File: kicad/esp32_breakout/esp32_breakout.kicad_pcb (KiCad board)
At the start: 2 copper layers, 85 x 39 mm, 29 parts, among them J1 JST PH F, J10 JST PH F, J11 JST PH F, J12 JST PH F, J13 JST PH F, J14 JST PH F, J2 JST PH F, J3 JST PH F, J4 DC-005 5.5x2.1mm, J5 Deans T-Plug M, J6 Header F, J7 Header F, J8 Header F, J9 JST PH F, Q1 BSS123, SW1 SS12D10, U1 ESP32 DEV KIT 30-pin, U2 Mini560-Pro

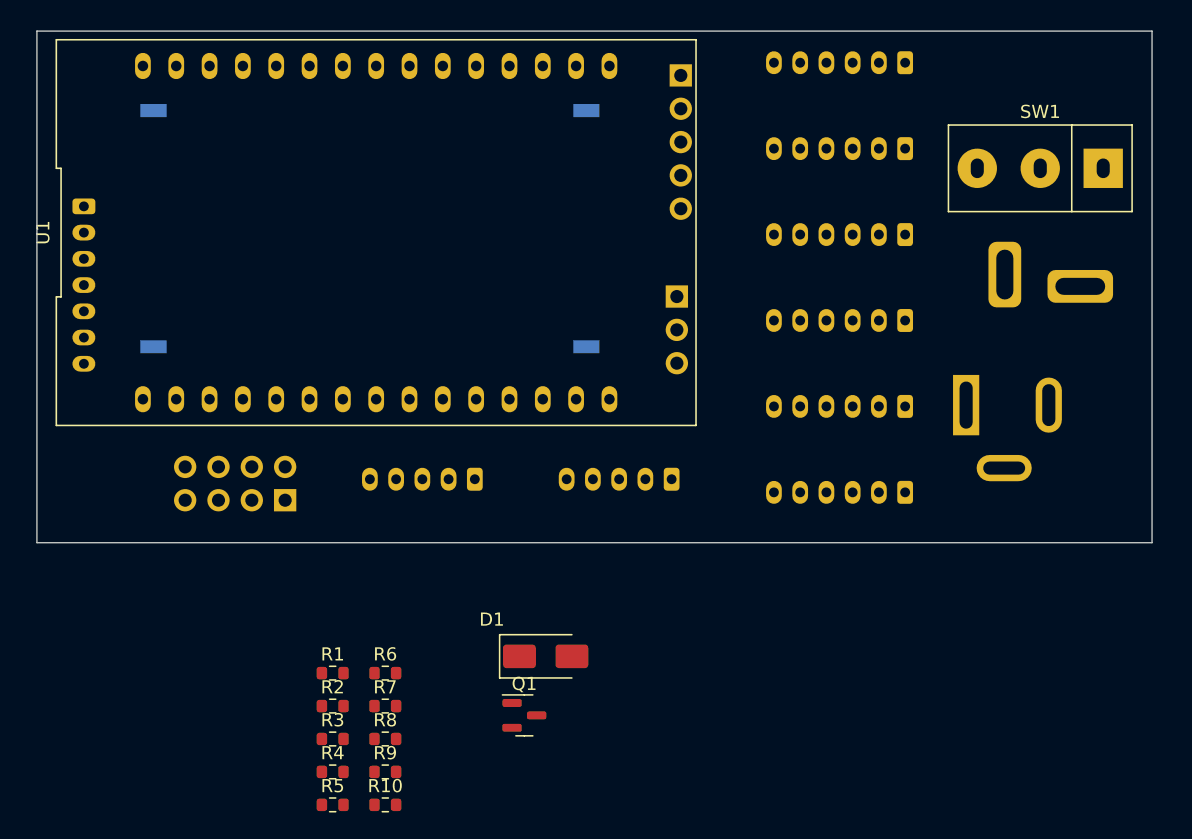
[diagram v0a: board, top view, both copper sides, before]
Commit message: Fix broken fw; ESP32 schematic
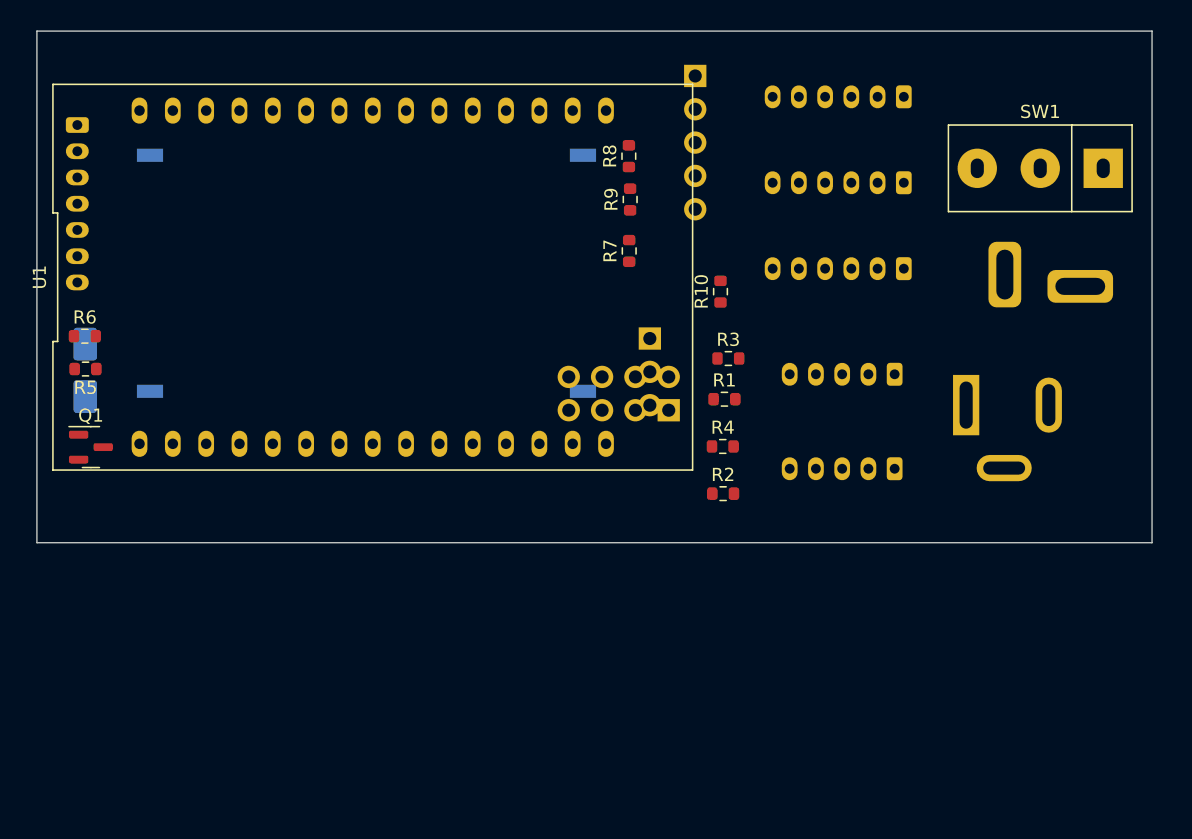
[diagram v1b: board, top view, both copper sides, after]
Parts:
- removed J12, J13, J14: JST PH F, Connector_JST:JST_PH_B6B-PH-K_1x06_P2.00mm_Vertical
- D1: moved to B.Cu
- moved R8 48.1 mm to (155.1, 87.4), turned to 90 degrees
- moved R9 47.5 mm to (155.2, 90.7), turned to 90 degrees
- moved R10 46.7 mm to (162.1, 97.7), turned to 90 degrees
- moved R3 41.8 mm to (162.7, 102.8)
- moved D1 41.3 mm to (113.7, 103.7), turned to 90 degrees
- moved R7 39.4 mm to (155.2, 94.6), turned to 90 degrees
- moved Q1 38.9 mm to (114.1, 109.5)
- moved R4 38.7 mm to (162.3, 109.5)
- moved R5 38.2 mm to (113.7, 103.6), turned to 180 degrees
- moved R1 36.4 mm to (162.4, 105.9)
- moved R6 34.4 mm to (113.7, 101.1)
- moved R2 33.9 mm to (162.3, 113.1)
- moved J1 32.0 mm to (175.4, 111.2)
- moved J6 30.0 mm to (158.2, 106.7)
- moved J2 18.8 mm to (175.4, 104.0)
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
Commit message: Layout DRC pass
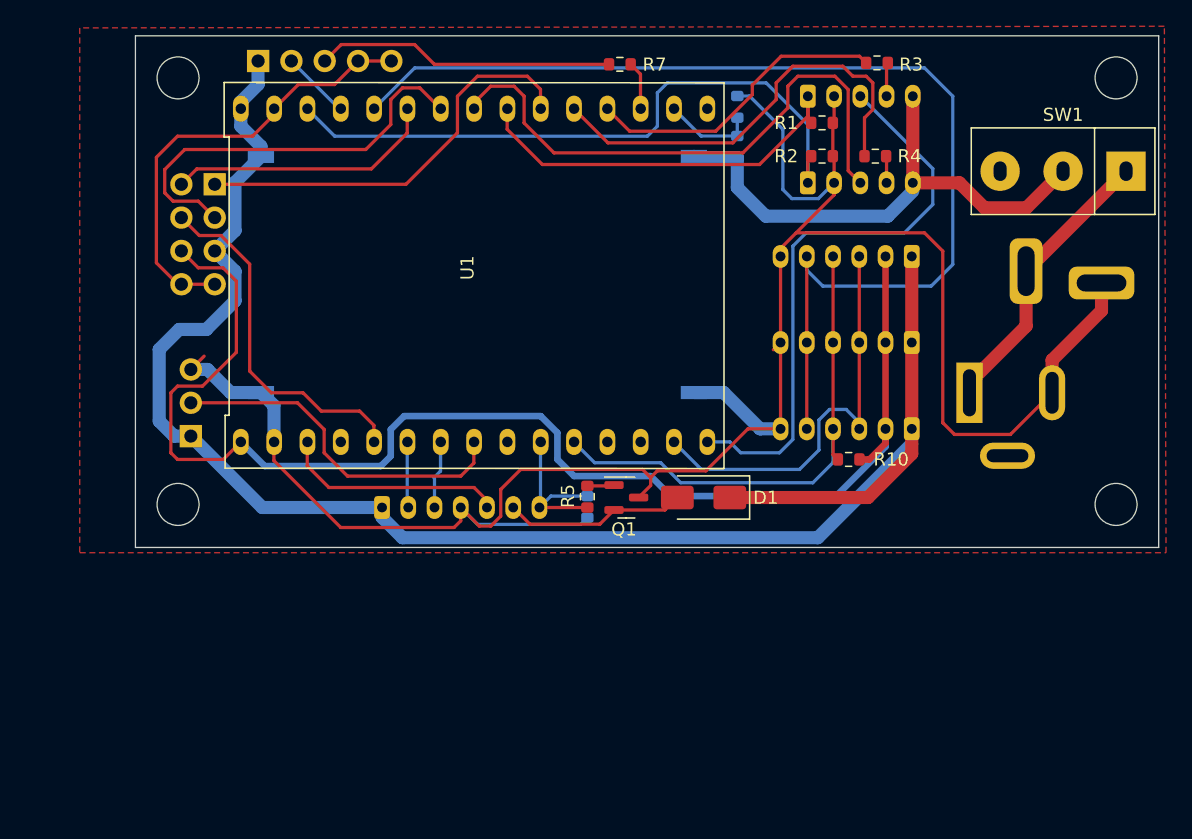
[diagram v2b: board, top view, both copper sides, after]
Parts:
- added H1: MountingHole, MountingHole:MountingHole_3.2mm_M3, F.Cu at (120.8, 81.4)
- added H2: MountingHole, MountingHole:MountingHole_3.2mm_M3, F.Cu at (192.3, 81.4)
- added H3: MountingHole, MountingHole:MountingHole_3.2mm_M3, F.Cu at (192.3, 113.9)
- added H4: MountingHole, MountingHole:MountingHole_3.2mm_M3, F.Cu at (120.8, 113.9)
- D1: moved to F.Cu
- R6, R8, R9: moved to B.Cu
- moved D1 48.1 mm to (160.8, 113.4), turned to 180 degrees
- moved Q1 41.0 mm to (154.9, 113.4)
- moved R6 40.5 mm to (152.0, 114.1), turned to -90 degrees
- moved R5 39.5 mm to (152.0, 113.3), turned to -90 degrees
- moved J6 38.7 mm to (123.6, 89.5), turned to 180 degrees
- moved J3 37.3 mm to (136.3, 114.2), turned to 0 degrees
- moved J8 35.8 mm to (121.8, 108.7), turned to 0 degrees
- moved J7 33.3 mm to (126.9, 80.1), turned to -90 degrees
- moved R2 26.8 mm to (169.9, 87.4)
- moved R3 25.2 mm to (174.1, 80.3)
- moved R4 25.0 mm to (173.9, 87.4)
- moved J1 22.8 mm to (168.8, 89.4), turned to 0 degrees
- moved R1 22.3 mm to (169.9, 84.8)
- moved J2 22.2 mm to (168.8, 82.8), turned to 0 degrees
- moved R10 16.1 mm to (171.9, 110.5), turned to 180 degrees
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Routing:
- net GND: track 0.00 -> 201.9 mm
- net +5V: track 0.00 -> 129.3 mm
- net +3V3: track 0.00 -> 103.6 mm
- net /I2C_INT: track 0.00 -> 85.9 mm
- net /MOT_PWM_RIGHT: track 0.00 -> 50.1 mm
- net /MOT_CW_LEFT: track 0.00 -> 44.7 mm
- net /MOT_CW_RIGHT: track 0.00 -> 44.1 mm
- net +24V: track 0.00 -> 41.3 mm
- net /I2C_SDA: track 0.00 -> 39.9 mm
- net /MOT_FG_RIGHT: track 0.00 -> 33.4 mm
- net /I2C_SCL: track 0.00 -> 33.0 mm
- net /GPIO32_TOUCH: track 0.00 -> 31.8 mm
- net /GPIO26_TOUCH: track 0.00 -> 31.7 mm
- net /MOT_PWM_LEFT: track 0.00 -> 30.8 mm
- net /GPIO4_TOUCH: track 0.00 -> 27.3 mm
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- added copper zone on F.Cu, net GND
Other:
- board size 85 x 39 mm -> 78 x 39 mm
